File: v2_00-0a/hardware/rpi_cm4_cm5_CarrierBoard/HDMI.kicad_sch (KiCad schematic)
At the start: 12 parts, among them J4 2086581001

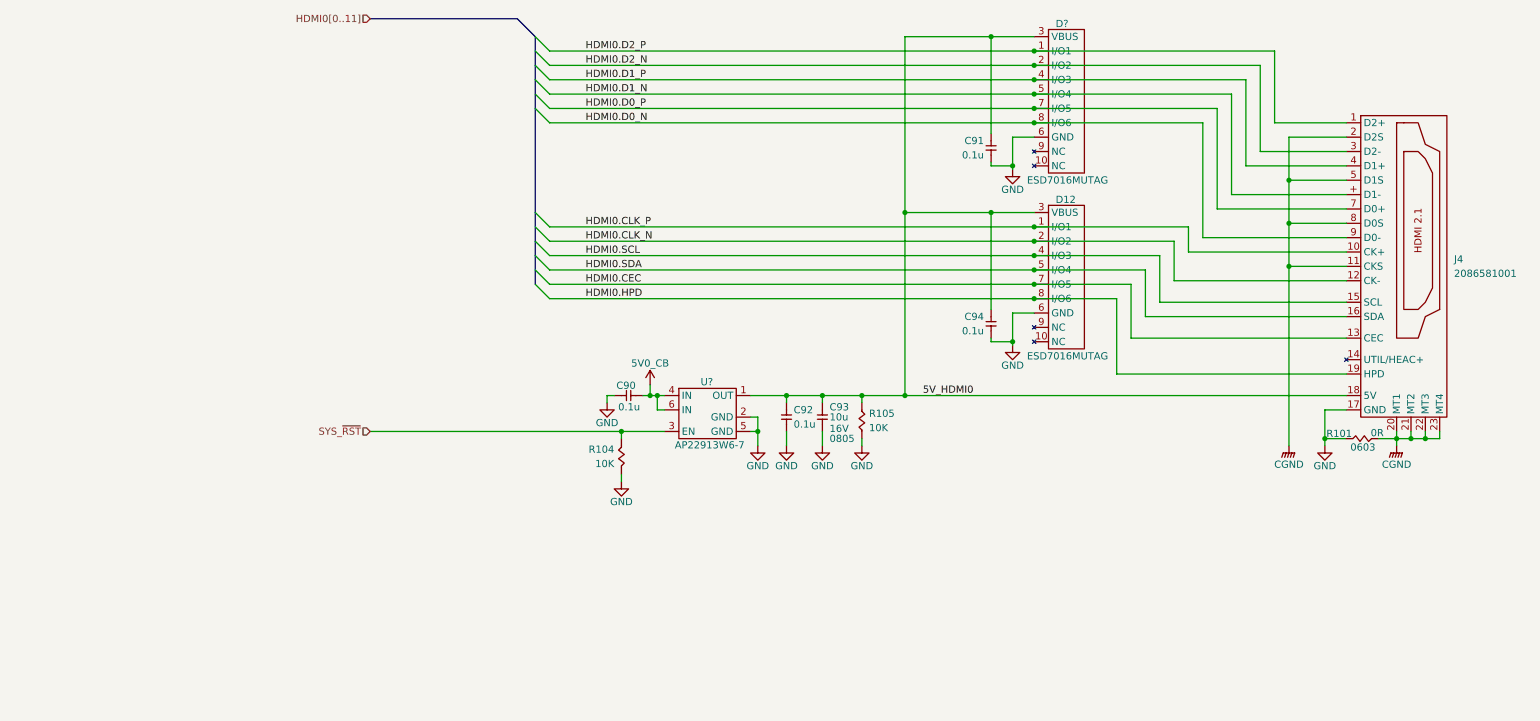
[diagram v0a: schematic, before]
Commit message: Update schematics (several new hierarchical pages, updates bus labels)
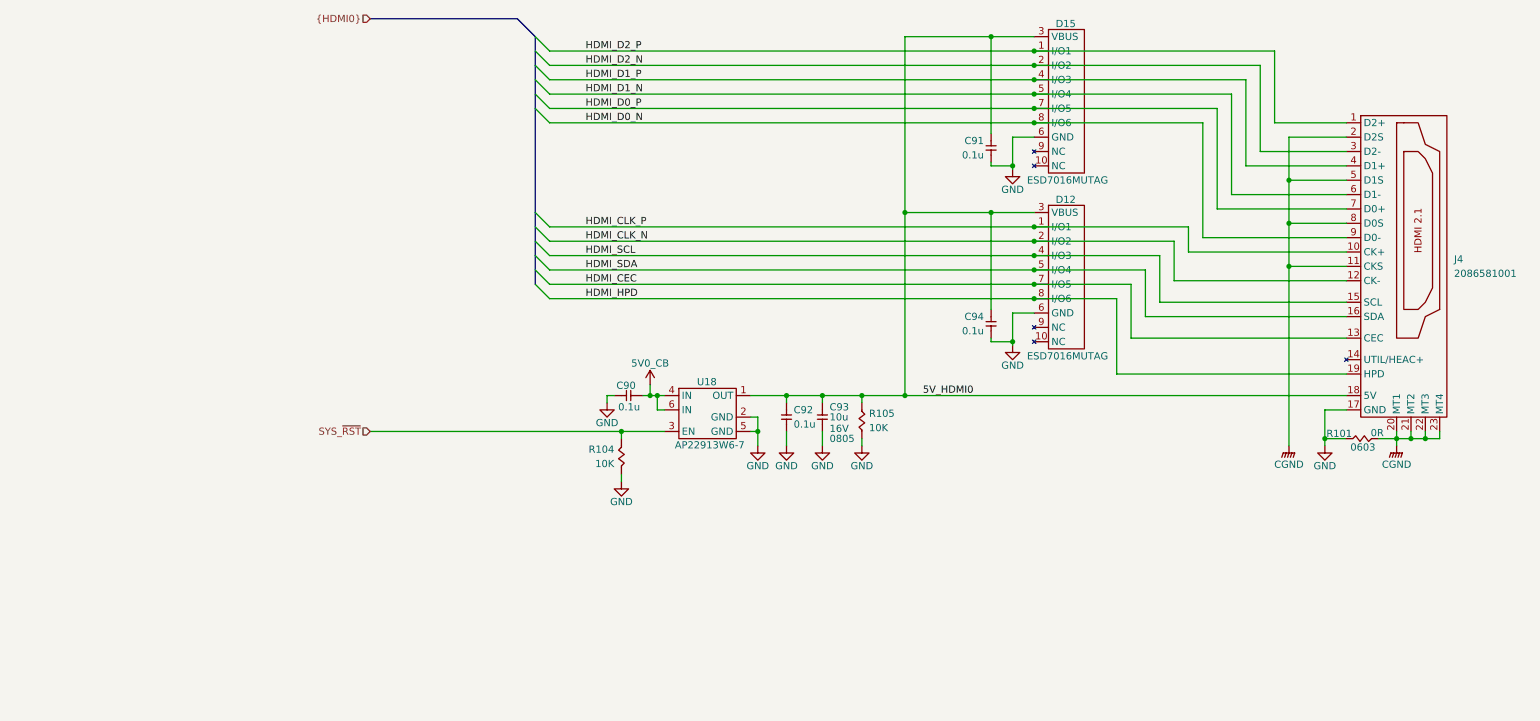
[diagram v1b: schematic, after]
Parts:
- removed D?: ESD7016MUTAG, footprint:UDFN8, symbol KicadCompDb:ESD Diodes/ESD_DIODE_00001
- removed U?: AP22913W6-7, footprint:SOT-23-6, symbol KicadCompDb:Load Switch/LOAD_SW_00001
- added D15: ESD7016MUTAG, footprint:UDFN8, symbol KicadCompDb:ESD Diodes/ESD_DIODE_00001
- added U18: AP22913W6-7, footprint:SOT-23-6, symbol KicadCompDb:Load Switch/LOAD_SW_00001
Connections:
- net 5V0_CB: now also U18.4 (IN), U18.6 (IN)
- net 5V_HDMI0: now also D15.3 (VBUS), U18.1 (OUT)
- net GND: now also D15.6 (GND), U18.2 (GND), U18.5 (GND)
- net SYS_~{RST}: now also U18.3 (EN)
- net HDMI0.CEC renamed HDMI_CEC
- net HDMI0.CLK_N renamed HDMI_CLK_N
- net HDMI0.CLK_P renamed HDMI_CLK_P
- net HDMI0.D0_N renamed HDMI_D0_N
- net HDMI_D0_N: now also D15.8 (I/O6)
- net HDMI0.D0_P renamed HDMI_D0_P
- net HDMI_D0_P: now also D15.7 (I/O5)
- removed net HDMI0.D1_N: J4.+ (D1-)
- net HDMI0.D1_P renamed HDMI_D1_P
- net HDMI_D1_P: now also D15.4 (I/O3)
- net HDMI0.D2_N renamed HDMI_D2_N
- net HDMI_D2_N: now also D15.2 (I/O2)
- net HDMI0.D2_P renamed HDMI_D2_P
- net HDMI_D2_P: now also D15.1 (I/O1)
- net HDMI0.HPD renamed HDMI_HPD
- net HDMI0.SCL renamed HDMI_SCL
- net HDMI0.SDA renamed HDMI_SDA
- new net HDMI_D1_N: D15.5 (I/O4), J4.6 (D1-)

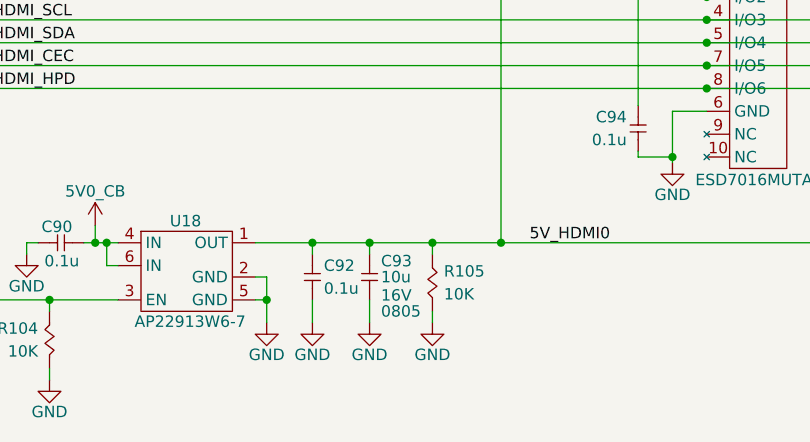
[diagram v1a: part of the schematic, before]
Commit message: Add new page and update schematics
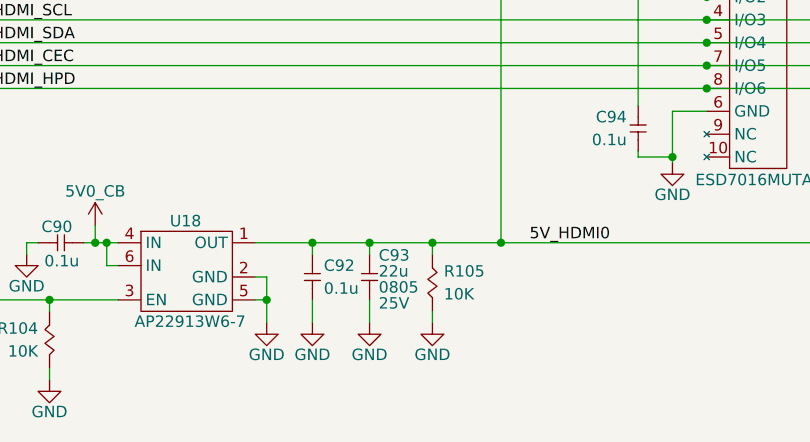
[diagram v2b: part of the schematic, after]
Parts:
- removed C93: 10u, footprint:CAP_NONPOL_0805, symbol KicadCompDb:Capacitors/CAP_CER_SMT_00004
- added C93: 22u, footprint:CAP_NONPOL_0805, symbol KicadCompDb:Capacitors/CAP_CER_SMT_00011
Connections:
- net 5V_HDMI0: now also C93.2
- net GND: now also C93.1
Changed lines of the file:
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@@
-	)
-	(symbol
-		(lib_id "KicadCompDb:Capacitors/CAP_CER_SMT_00004")
-		(at 156.21 123.825 90)
-		(unit 1)
-		(exclude_from_sim no)
-		(in_bom yes)
-		(on_board yes)
-		(dnp no)
-		(property "Reference" "C93"
-			(at 157.48 119.507 90)
-			(effects
-				(font
-					(size 1.27 1.27)
-				)
-				(justify right)
-			)
-		)
-		(property "Value" "10u"
-			(at 157.48 121.285 90)
-			(effects
-				(font
-					(size 1.27 1.27)
-				)
-				(justify right)
-			)
-		)
-		(property "Footprint" "footprint:CAP_NONPOL_0805"
-			(at 178.308 123.317 0)
-			(effects
-				(font
-					(size 1.27 1.27)
-				)
-				(hide yes)
-			)
-		)
-		(property "Datasheet" "https://mm.digikey.com/Volume0/opasdata/d220001/medias/docus/609/CL21A106KOQNNNE_Spec.pdf"
-			(at 156.21 123.825 0)
-			(effects
-				(font
-					(size 1.27 1.27)
-				)
-				(hide yes)
-			)
-		)
-		(property "Description" "CAP CER 10UF 16V X5R 0805"
-			(at 166.116 122.047 0)
-			(effects
-				(font
-					(size 1.27 1.27)
-				)
-				(hide yes)
-			)
-		)
-		(property "Tolerance" "±10%"
-			(at 176.53 123.571 0)
-			(effects
-				(font
-					(size 1.27 1.27)
-				)
-				(hide yes)
-			)
-		)
-		(property "Dielectric" "X5R"
-			(at 170.434 123.571 0)
-			(effects
-				(font
-					(size 1.27 1.27)
-				)
-				(hide yes)
-			)
-		)
-		(property "Package" "0805"
-			(at 157.48 125.095 90)
-			(effects
-				(font
-					(size 1.27 1.27)
-				)
-				(justify right)
-			)
-		)
-		(property "Operating Temperature" "-55°C ~ 85°C"
-			(at 180.594 123.063 0)
-			(effects
-				(font
-					(size 1.27 1.27)
-				)
-				(hide yes)
-			)
-		)
-		(property "Voltage Rating" "16V"
-			(at 157.48 123.317 90)
-			(effects
-				(font
-					(size 1.27 1.27)
-				)
-				(justify right)
-			)
-		)
-		(property "Manufacturer" "Samsung Electro-Mechanics"
-			(at 174.498 123.571 0)
-			(effects
-				(font
-					(size 1.27 1.27)
-				)
-				(hide yes)
-			)
-		)
-		(property "Manufacturer Part Number" "CL21A106KOQNNNE"
-			(at 164.084 123.571 0)
-			(effects
-				(font
-					(size 1.27 1.27)
-				)
-				(hide yes)
-			)
-		)
-		(property "Distributor" "DigiKey"
-			(at 162.052 123.825 0)
-			(effects
-				(font
-					(size 1.27 1.27)
-				)
-				(hide yes)
-			)
-		)
-		(property "Distributor Part Number" "1276-1096-1-ND"
-			(at 168.402 123.063 0)
-			(effects
-				(font
-					(size 1.27 1.27)
-				)
-				(hide yes)
-			)
-		)
-		(property "Type" "CER SMT"
-			(at 156.21 123.825 0)
-			(show_name yes)
-			(effects
-				(font
-					(size 1.27 1.27)
-				)
-				(hide yes)
-			)
-		)
-		(property "Dimensions" "2.00mm x 1.25mm"
-			(at 156.21 123.825 0)
-			(show_name yes)
-			(effects
-				(font
-					(size 1.27 1.27)
-				)
-				(hide yes)
-			)
-		)
-		(pin "2"
-		)
-		(pin "1"
-		)
-		(instances
-			(project "rpi_cm4_cm5_CarrierBoard"
-				(path "/7dcdf741-90ca-4333-848c-806f4d64158e/da79d379-819b-4a23-bde6-cf0346f2b26a"
-					(reference "C93")
-					(unit 1)
-				)
-			)
-		)
 	)
 	(symbol
@@
 					(unit 1)
 				)
+			)
+		)
+	)
+	(symbol
+		(lib_id "KicadCompDb:Capacitors/CAP_CER_SMT_00011")
+		(at 156.21 123.825 90)
+		(unit 1)
+		(exclude_from_sim no)
+		(in_bom yes)
+		(on_board yes)
+		(dnp no)
+		(property "Reference" "C93"
+			(at 157.226 118.872 90)
+			(effects
+				(font
+					(size 1.27 1.27)
+				)
+				(justify right)
+			)
+		)
+		(property "Value" "22u"
+			(at 157.226 120.65 90)
+			(effects
+				(font
+					(size 1.27 1.27)
+				)
+				(justify right)
+			)
+		)
+		(property "Footprint" "footprint:CAP_NONPOL_0805"
+			(at 178.308 123.317 0)
+			(effects
+				(font
+					(size 1.27 1.27)
+				)
+				(hide yes)
+			)
+		)
+		(property "Datasheet" "https://mm.digikey.com/Volume0/opasdata/d220001/medias/docus/339/CL21A226MAYNNNE_Spec.pdf"
+			(at 156.21 123.825 0)
+			(effects
+				(font
+					(size 1.27 1.27)
+				)
+				(hide yes)
+			)
+		)
+		(property "Description" "CAP CER 22UF 25V X5R 0805"
+			(at 166.116 122.047 0)
+			(effects
+				(font
+					(size 1.27 1.27)
+				)
+				(hide yes)
+			)
+		)
+		(property "Tolerance" "±20%"
+			(at 176.53 123.571 0)
+			(effects
+				(font
+					(size 1.27 1.27)
+				)
+				(hide yes)
+			)
+		)
+		(property "Dielectric" "X5R"
+			(at 170.434 123.571 0)
+			(effects
+				(font
+					(size 1.27 1.27)
+				)
+				(hide yes)
+			)
+		)
+		(property "Package" "0805"
+			(at 157.226 122.428 90)
+			(effects
+				(font
+					(size 1.27 1.27)
+				)
+				(justify right)
+			)
+		)
+		(property "Operating Temperature" "-55°C ~ 85°C"
+			(at 180.594 123.063 0)
+			(effects
+				(font
+					(size 1.27 1.27)
+				)
+				(hide yes)
+			)
+		)
+		(property "Voltage Rating" "25V"
+			(at 157.226 124.206 90)
+			(effects
+				(font
+					(size 1.27 1.27)
+				)
+				(justify right)
+			)
+		)
+		(property "Manufacturer" "Samsung Electro-Mechanics"
+			(at 174.498 123.571 0)
+			(effects
+				(font
+					(size 1.27 1.27)
+				)
+				(hide yes)
+			)
+		)
+		(property "Manufacturer Part Number" "CL21A226MAYNNNE"
+			(at 164.084 123.571 0)
+			(effects
+				(font
+					(size 1.27 1.27)
+				)
+				(hide yes)
+			)
+		)
+		(property "Distributor" "DigiKey"
+			(at 162.052 123.825 0)
+			(effects
+				(font
+					(size 1.27 1.27)
+				)
+				(hide yes)
+			)
+		)
+		(property "Distributor Part Number" "1276-CL21A226MAYNNNECT-ND"
+			(at 168.402 123.063 0)
+			(effects
+				(font
+					(size 1.27 1.27)
+				)
+				(hide yes)
+			)
+		)
+		(property "Type" "CER SMT"
+			(at 156.21 123.825 0)
+			(show_name yes)
+			(effects
+				(font
+					(size 1.27 1.27)
+				)
+				(hide yes)
+			)
+		)
+		(property "Dimensions" "2.00mm x 1.25mm"
+			(at 156.21 123.825 0)
+			(show_name yes)
+			(effects
+				(font
+					(size 1.27 1.27)
+				)
+				(hide yes)
+			)
+		)
+		(pin "1"
+		)
+		(pin "2"
+		)
+		(instances
+			(project "rpi_cm4_cm5_CarrierBoard"
+				(path "/7dcdf741-90ca-4333-848c-806f4d64158e/da79d379-819b-4a23-bde6-cf0346f2b26a"
+					(reference "C93")
+					(unit 1)
+				)

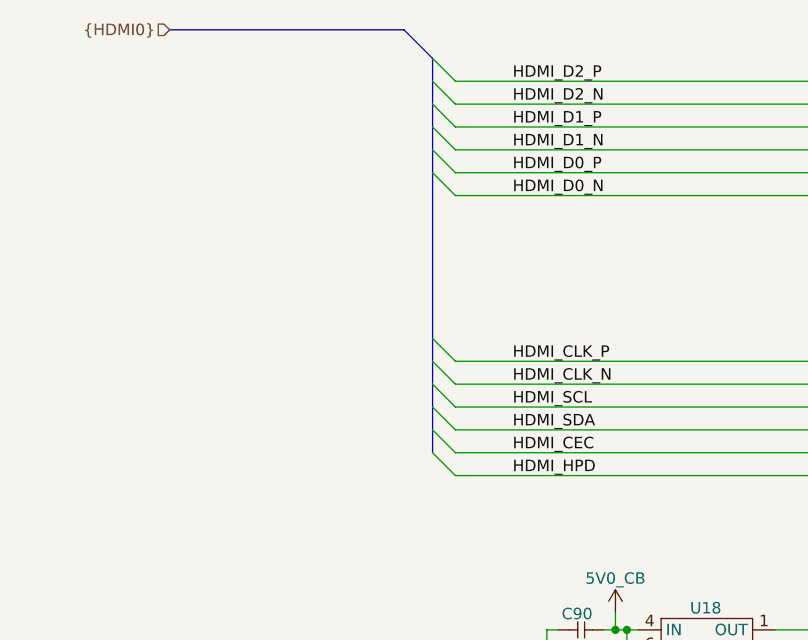
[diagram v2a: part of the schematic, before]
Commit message: Add design notes (power table) and latest changes to power supply and power input
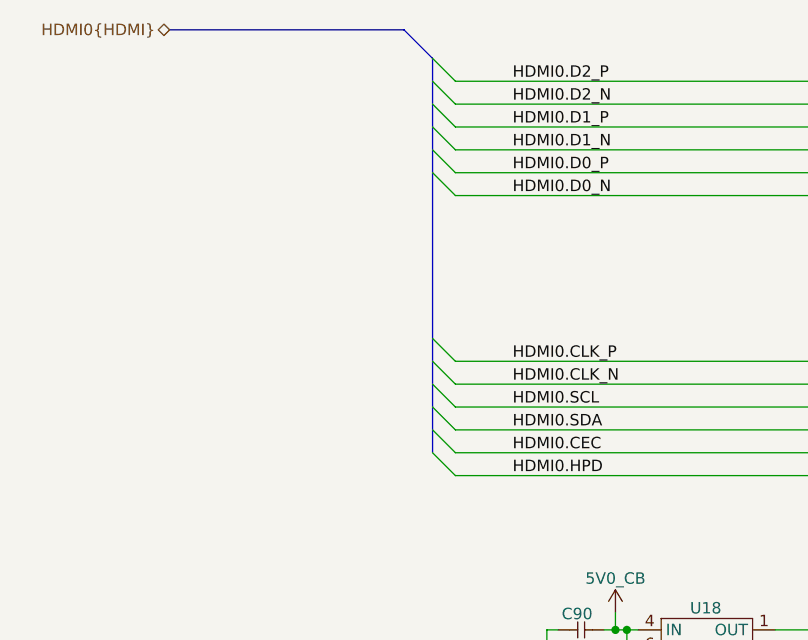
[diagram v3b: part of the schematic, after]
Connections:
- net HDMI_CEC renamed HDMI0.CEC
- net HDMI_CLK_N renamed HDMI0.CLK_N
- net HDMI_CLK_P renamed HDMI0.CLK_P
- net HDMI_D0_N renamed HDMI0.D0_N
- net HDMI_D0_P renamed HDMI0.D0_P
- net HDMI_D1_N renamed HDMI0.D1_N
- net HDMI_D1_P renamed HDMI0.D1_P
- net HDMI_D2_N renamed HDMI0.D2_N
- net HDMI_D2_P renamed HDMI0.D2_P
- net HDMI_HPD renamed HDMI0.HPD
- net HDMI_SCL renamed HDMI0.SCL
- net HDMI_SDA renamed HDMI0.SDA
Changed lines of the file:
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@@
 		(comment 8 "WIP")
 	)
-	(bus_alias "HDMI0"
-		(members "HDMI_D0_P" "HDMI_D0_N" "HDMI_D1_P" "HDMI_D1_N" "HDMI_D2_P" "HDMI_D2_N"
-			"HDMI_CLK_P" "HDMI_CLK_N" "HDMI_SDA" "HDMI_SCL" "HDMI_CEC" "HDMI_HPD"
+	(bus_alias "HDMI"
+		(members "D0_P" "D0_N" "D1_P" "D1_N" "D2_P" "D2_N" "CLK_P" "CLK_N" "SDA"
+			"SCL" "CEC" "HPD"
 		)
 	)
@@
 		)
 	)
-	(label "HDMI_D0_N"
+	(label "HDMI0.D0_N"
 		(at 114.3 69.215 0)
 		(effects
@@
 		)
 	)
-	(label "HDMI_CEC"
+	(label "HDMI0.CEC"
 		(at 114.3 97.79 0)
 		(effects
@@
 		)
 	)
-	(label "HDMI_HPD"
+	(label "HDMI0.HPD"
 		(at 114.3 100.33 0)
 		(effects
@@
 		)
 	)
-	(label "HDMI_SCL"
+	(label "HDMI0.SCL"
 		(at 114.3 92.71 0)
 		(effects
@@
 		)
 	)
-	(label "HDMI_CLK_P"
+	(label "HDMI0.CLK_P"
 		(at 114.3 87.63 0)
 		(effects
@@
 		)
 	)
-	(label "HDMI_SDA"
+	(label "HDMI0.SDA"
 		(at 114.3 95.25 0)
 		(effects
@@
 		)
 	)
-	(label "HDMI_D0_P"
+	(label "HDMI0.D0_P"
 		(at 114.3 66.675 0)
 		(effects
@@
 		)
 	)
-	(label "HDMI_D1_P"
+	(label "HDMI0.D1_P"
 		(at 114.3 61.595 0)
 		(effects
@@
 		)
 	)
-	(label "HDMI_D2_P"
+	(label "HDMI0.D2_P"
 		(at 114.3 56.515 0)
 		(effects
@@
 		)
 	)
-	(label "HDMI_CLK_N"
+	(label "HDMI0.CLK_N"
 		(at 114.3 90.17 0)
 		(effects
@@
 		)
 	)
-	(label "HDMI_D1_N"
+	(label "HDMI0.D1_N"
 		(at 114.3 64.135 0)
 		(effects
@@
 		)
 	)
-	(label "HDMI_D2_N"
+	(label "HDMI0.D2_N"
 		(at 114.3 59.055 0)
 		(effects
@@
 		)
 	)
-	(hierarchical_label "{HDMI0}"
-		(shape input)
+	(hierarchical_label "HDMI0{HDMI}"
+		(shape bidirectional)
 		(at 76.2 50.8 180)
 		(effects

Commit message: Add and modify existing schematics
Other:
- note added: "Resistors are 1% 1/16W 0402 unless otherwise noted Capacitors are 10% 50V X7R 0402 unless otherwise noted"
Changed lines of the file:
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@@
+		)
+	)
+	(text "Resistors are 1% 1/16W 0402 unless otherwise noted\nCapacitors are 10% 50V X7R 0402 unless otherwise noted"
+		(exclude_from_sim no)
+		(at 12.7 170.942 0)
+		(effects
+			(font
+				(size 1.27 1.27)
+			)
+			(justify left)
 		)
 	)
